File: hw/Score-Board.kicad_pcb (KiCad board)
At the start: 2 copper layers, 184.2 x 81.3 mm, 97 parts, among them J1 Barrel_Jack, J2 Screw_Terminal_01x02, J3 SPI-Disp, J4 Conn_01x03, J5 Conn_01x04, J6 J-V3.3, J7 J-V12, J8 J-VSYS, Q1 2N3904, Q10 2N3905, Q11 2N3905, Q12 2N3905, Q13 2N3905, Q14 2N3905, Q15 2N3904, Q16 2N3904, Q17 2N3904, Q18 2N3904, Q19 2N3904, Q2 2N3904, Q20 2N3904, Q21 2N3904, Q22 2N3904, Q3 2N3904, Q4 2N3904, Q5 2N3904, Q6 2N3904, Q7 2N3904, Q8 2N3905, Q9 2N3905, SW1 RESET, SW2 NETWORK, SW3 INPUT-SW, U1 PicoW, U2 E18-MS1-PCB, U5 MCP1702-5002E

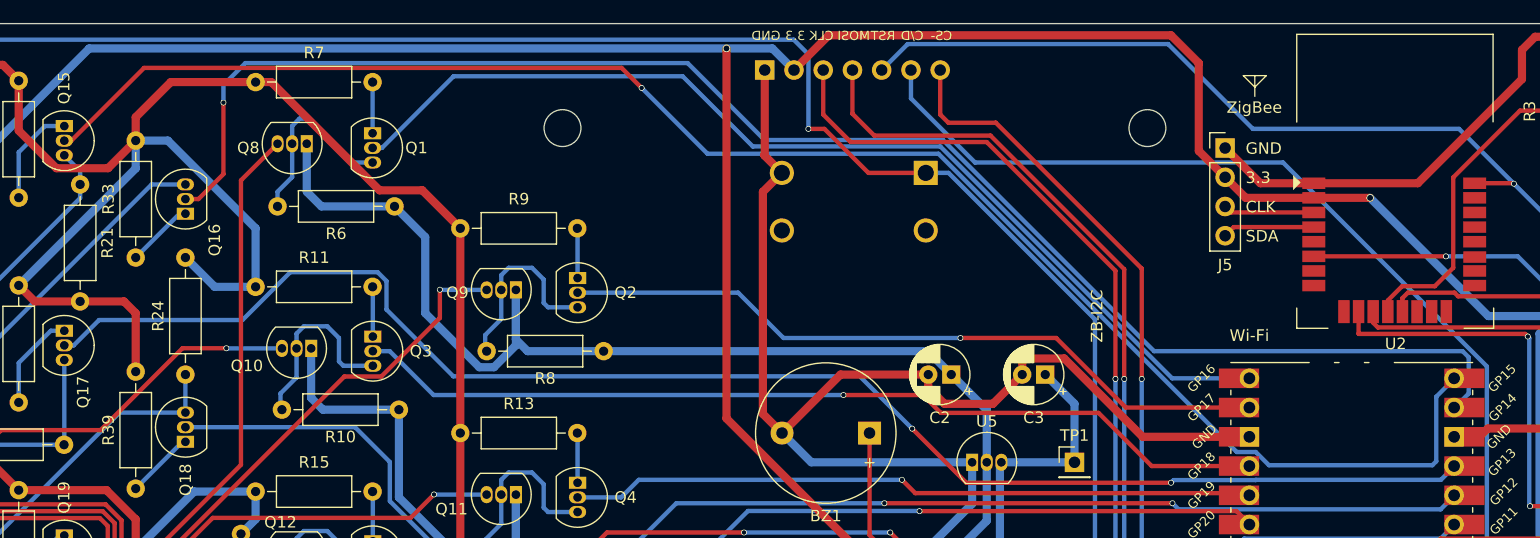
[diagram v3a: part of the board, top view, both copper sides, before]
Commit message: Add board cutout for Wi-Fi ant area of Pico-W.
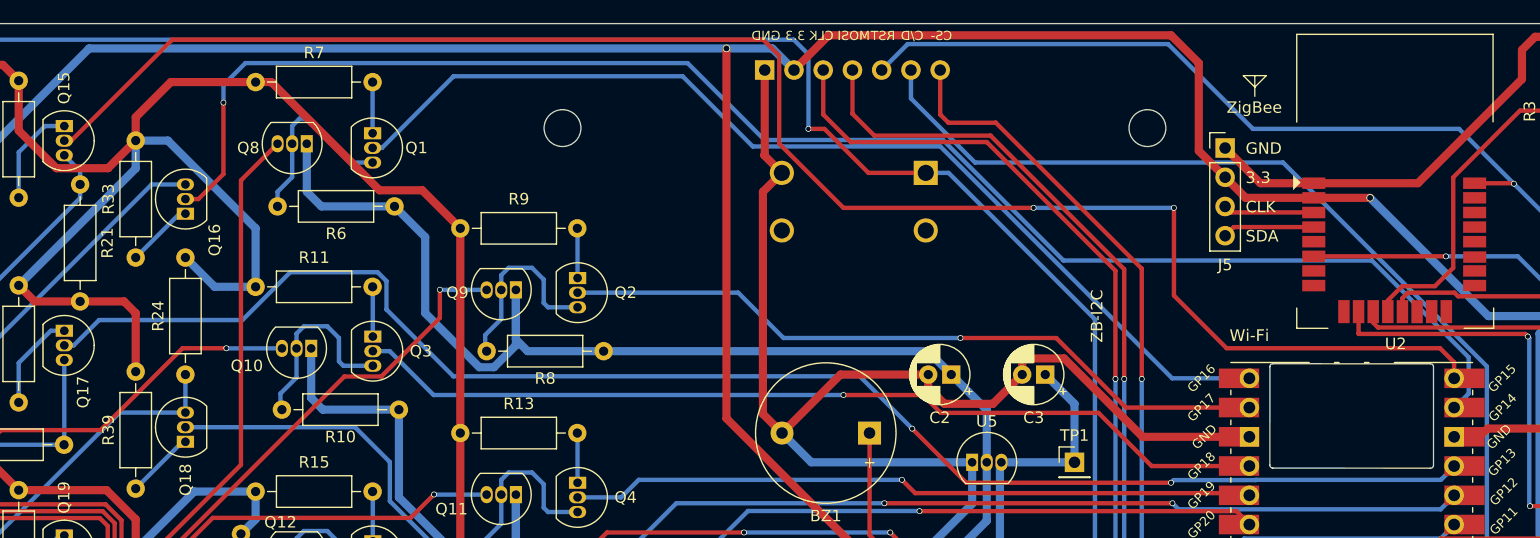
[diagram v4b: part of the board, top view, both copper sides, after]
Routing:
- net /SE.A: track 144.1 -> 146.3 mm, vias 1 -> 2
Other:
- outline, holes or cut-outs redrawn
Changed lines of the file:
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@@
       (outputformat 1)
       (mirror false)
-      (drillshape 1)
+      (drillshape 0)
       (scaleselection 1)
       (outputdirectory "")
@@
   (gr_circle (center 122.084 107.482) (end 122.853914 107.482)
     (stroke (width 0.15) (type solid)) (fill solid) (layer "F.SilkS"))
+  (gr_line (start 181.963125 80.565499) (end 168.267348 80.5505)
+    (stroke (width 0.1) (type default)) (layer "Edge.Cuts"))
   (gr_line (start 224.065 44.49) (end 224.065 120.69)
     (stroke (width 0.1) (type default)) (layer "Edge.Cuts"))
   (gr_arc (start 221.525 41.95) (mid 223.321051 42.693949) (end 224.065 44.49)
     (stroke (width 0.1) (type default)) (layer "Edge.Cuts"))
+  (gr_arc (start 182.219175 80.305176) (mid 182.146282 80.489564) (end 181.963125 80.565499)
+    (stroke (width 0.1) (type default)) (layer "Edge.Cuts"))
   (gr_line (start 42.455 41.95) (end 221.525 41.95)
     (stroke (width 0.1) (type default)) (layer "Edge.Cuts"))
+  (gr_line (start 168.265489 71.49214) (end 181.957465 71.496443)
+    (stroke (width 0.1) (type default)) (layer "Edge.Cuts"))
+  (gr_arc (start 168.267348 80.5505) (mid 168.08296 80.477607) (end 168.007025 80.29445)
+    (stroke (width 0.1) (type default)) (layer "Edge.Cuts"))
+  (gr_arc (start 168.009439 71.752463) (mid 168.082332 71.568075) (end 168.265489 71.49214)
+    (stroke (width 0.1) (type default)) (layer "Edge.Cuts"))
   (gr_line (start 39.915 120.69) (end 39.915 44.49)
     (stroke (width 0.1) (type default)) (layer "Edge.Cuts"))
   (gr_arc (start 42.455 123.23) (mid 40.658949 122.486051) (end 39.915 120.69)
     (stroke (width 0.1) (type default)) (layer "Edge.Cuts"))
+  (gr_line (start 182.217788 71.752493) (end 182.219175 80.305176)
+    (stroke (width 0.1) (type default)) (layer "Edge.Cuts"))
   (gr_arc (start 224.068173 120.69) (mid 223.323295 122.488295) (end 221.525 123.233173)
     (stroke (width 0.1) (type default)) (layer "Edge.Cuts"))
+  (gr_line (start 168.007025 80.29445) (end 168.009439 71.752463)
+    (stroke (width 0.1) (type default)) (layer "Edge.Cuts"))
+  (gr_arc (start 181.957465 71.496443) (mid 182.141853 71.569336) (end 182.217788 71.752493)
+    (stroke (width 0.1) (type default)) (layer "Edge.Cuts"))
   (gr_line (start 221.525 123.233173) (end 42.455 123.233173)
     (stroke (width 0.1) (type default)) (layer "Edge.Cuts"))
@@
   (segment (start 61.625 50.847) (end 63.304 50.847) (width 0.381) (layer "B.Cu") (net 57))
   (segment (start 59.346 53.126) (end 61.625 50.847) (width 0.381) (layer "B.Cu") (net 57))
-  (segment (start 111.7082 45.7982) (end 70.2298 45.7982) (width 0.381) (layer "F.Cu") (net 58))
+  (segment (start 124.012118 43.347) (end 72.681 43.347) (width 0.381) (layer "F.Cu") (net 58))
+  (segment (start 130.974 57.952) (end 147.484 57.952) (width 0.381) (layer "F.Cu") (net 58))
+  (segment (start 164.248 70.144) (end 182.79 70.144) (width 0.381) (layer "F.Cu") (net 58))
+  (segment (start 125.393637 52.371637) (end 125.393637 44.728519) (width 0.381) (layer "F.Cu") (net 58))
+  (segment (start 130.974 57.952) (end 125.393637 52.371637) (width 0.381) (layer "F.Cu") (net 58))
+  (segment (start 159.676 65.572) (end 164.248 70.144) (width 0.381) (layer "F.Cu") (net 58))
+  (segment (start 184.0091 71.3631) (end 184.0091 72.756) (width 0.381) (layer "F.Cu") (net 58))
+  (segment (start 125.393637 44.728519) (end 124.012118 43.347) (width 0.381) (layer "F.Cu") (net 58))
+  (segment (start 72.681 43.347) (end 63.911 52.117) (width 0.381) (layer "F.Cu") (net 58))
+  (segment (start 159.676 57.952) (end 159.676 65.572) (width 0.381) (layer "F.Cu") (net 58))
   (segment (start 63.911 52.117) (end 63.304 52.117) (width 0.381) (layer "F.Cu") (net 58))
-  (segment (start 70.2298 45.7982) (end 63.911 52.117) (width 0.381) (layer "F.Cu") (net 58))
-  (segment (start 113.448 47.538) (end 111.7082 45.7982) (width 0.381) (layer "F.Cu") (net 58))
-  (via (at 113.448 47.538) (size 0.508) (drill 0.381) (layers "F.Cu" "B.Cu") (net 58))
-  (segment (start 166.784637 79.1577) (end 167.930937 80.304) (width 0.381) (layer "B.Cu") (net 58))
-  (segment (start 165.1337 79.1577) (end 166.784637 79.1577) (width 0.381) (layer "B.Cu") (net 58))
-  (segment (start 182.4605 74.3555) (end 184.06 72.756) (width 0.381) (layer "B.Cu") (net 58))
-  (segment (start 139.229 53.253) (end 165.1337 79.1577) (width 0.381) (layer "B.Cu") (net 58))
-  (segment (start 182.120657 80.304) (end 182.4605 79.964157) (width 0.381) (layer "B.Cu") (net 58))
-  (segment (start 113.448 47.538) (end 119.163 53.253) (width 0.381) (layer "B.Cu") (net 58))
-  (segment (start 119.163 53.253) (end 139.229 53.253) (width 0.381) (layer "B.Cu") (net 58))
-  (segment (start 182.4605 79.964157) (end 182.4605 74.3555) (width 0.381) (layer "B.Cu") (net 58))
-  (segment (start 167.930937 80.304) (end 182.120657 80.304) (width 0.381) (layer "B.Cu") (net 58))
+  (segment (start 182.79 70.144) (end 184.0091 71.3631) (width 0.381) (layer "F.Cu") (net 58))
+  (via (at 147.484 57.952) (size 0.508) (drill 0.381) (layers "F.Cu" "B.Cu") (net 58))
+  (via (at 159.676 57.952) (size 0.508) (drill 0.381) (layers "F.Cu" "B.Cu") (net 58))
+  (segment (start 147.484 57.952) (end 159.676 57.952) (width 0.381) (layer "B.Cu") (net 58))
   (segment (start 69.506 62.27) (end 73.316 58.46) (width 0.381) (layer "B.Cu") (net 59))
   (segment (start 77.126 55.019) (end 74.955 57.19) (width 0.381) (layer "F.Cu") (net 60))
@@
   (segment (start 74.955 57.19) (end 73.824 57.19) (width 0.381) (layer "F.Cu") (net 60))
   (via (at 77.126 48.808) (size 0.508) (drill 0.381) (layers "F.Cu" "B.Cu") (net 60))
-  (segment (start 139.615724 52.0592) (end 124.121725 52.0592) (width 0.381) (layer "B.Cu") (net 60))
-  (segment (start 184.06 75.296) (end 185.2783 74.0777) (width 0.381) (layer "B.Cu") (net 60))
+  (segment (start 185.2783 70.933362) (end 176.868938 62.524) (width 0.381) (layer "B.Cu") (net 60))
   (segment (start 124.121725 52.0592) (end 117.441026 45.378501) (width 0.381) (layer "B.Cu") (net 60))
   (segment (start 79.031499 45.378501) (end 77.126 47.284) (width 0.381) (layer "B.Cu") (net 60))
-  (segment (start 157.954524 70.398) (end 139.615724 52.0592) (width 0.381) (layer "B.Cu") (net 60))
+  (segment (start 139.615724 52.0592) (end 124.121725 52.0592) (width 0.381) (layer "B.Cu") (net 60))
+  (segment (start 150.080524 62.524) (end 139.615724 52.0592) (width 0.381) (layer "B.Cu") (net 60))
+  (segment (start 117.441026 45.378501) (end 79.031499 45.378501) (width 0.381) (layer "B.Cu") (net 60))
   (segment (start 77.126 47.284) (end 77.126 48.808) (width 0.381) (layer "B.Cu") (net 60))
+  (segment (start 184.06 75.296) (end 185.2783 74.0777) (width 0.381) (layer "B.Cu") (net 60))
   (segment (start 185.2783 74.0777) (end 185.2783 70.933362) (width 0.381) (layer "B.Cu") (net 60))
-  (segment (start 184.742938 70.398) (end 157.954524 70.398) (width 0.381) (layer "B.Cu") (net 60))
-  (segment (start 185.2783 70.933362) (end 184.742938 70.398) (width 0.381) (layer "B.Cu") (net 60))
-  (segment (start 117.441026 45.378501) (end 79.031499 45.378501) (width 0.381) (layer "B.Cu") (net 60))
+  (segment (start 176.868938 62.524) (end 150.080524 62.524) (width 0.381) (layer "B.Cu") (net 60))
   (segment (start 62.133 68.627) (end 63.304 68.627) (width 0.381) (layer "B.Cu") (net 61))
   (segment (start 59.346 74.85) (end 59.346 71.414) (width 0.381) (layer "B.Cu") (net 61))
@@
       )
     )
-  )
-  (zone (net 0) (net_name "") (layers "F&B.Cu" "Dwgs.User") (name "Wi-Fi") (hatch full 0.5)
-    (connect_pads (clearance 0))
-    (min_thickness 0.25) (filled_areas_thickness no)
-    (keepout (tracks not_allowed) (vias not_allowed) (pads not_allowed) (copperpour allowed) (footprints allowed))
-    (fill (thermal_gap 0.5) (thermal_bridge_width 0.5))
-    (polygon
-      (pts
-        (xy 168.051952 71.414)
-        (xy 182.27 71.414)
-        (xy 182.27 71.414)
-        (xy 182.27 79.886)
-        (xy 182.270751 79.885249)
-        (xy 168.085049 79.895951)
-      )
-    )
